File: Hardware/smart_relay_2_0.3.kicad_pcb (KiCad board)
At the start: 2 copper layers, 39 parts, among them J1 UART1 PROGRAMMER, J3 Conn_01x07_Pin, K1 PB766-ND, K2 PB766-ND, Q1 NPN, Q2 NPN, Q3 NPN, Q4 NPN, U1 ESP32-WROOM-32E-N8, U2 Reg linear 3.3v

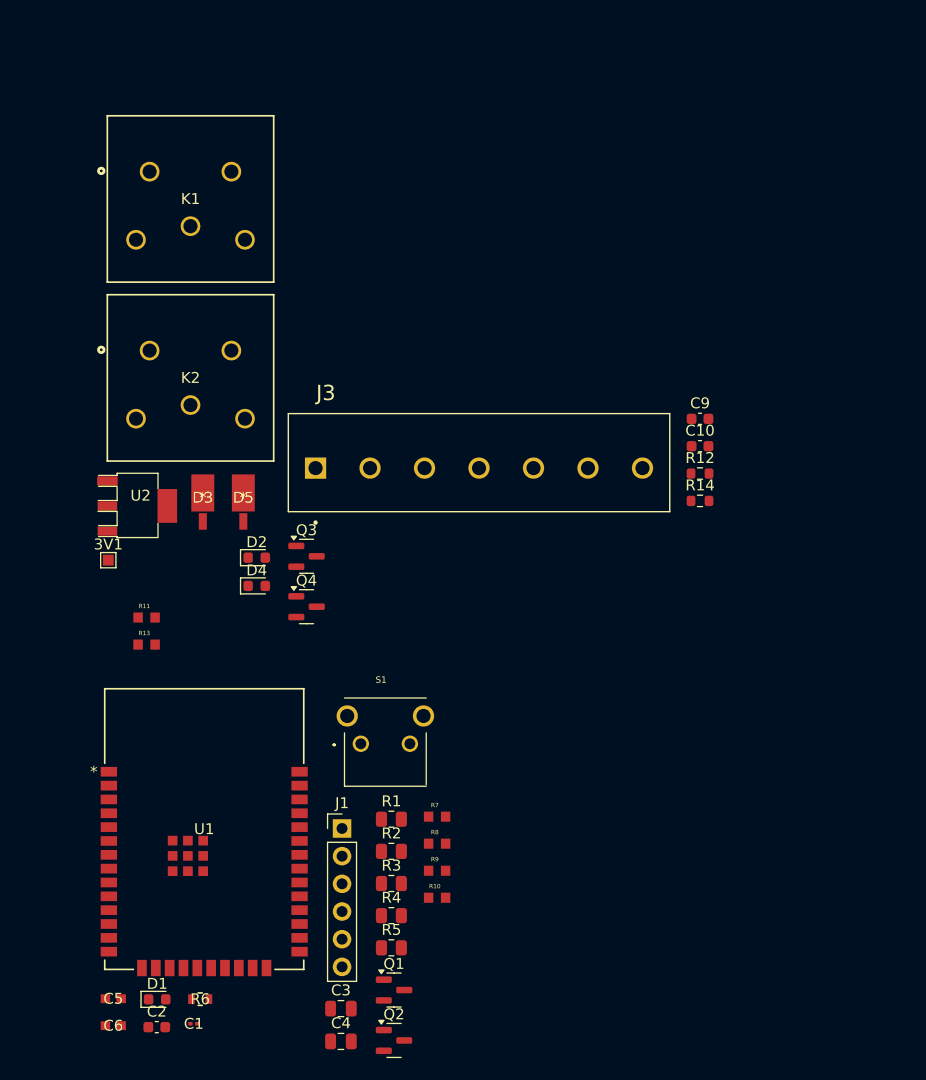
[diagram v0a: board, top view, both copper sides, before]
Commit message: strarted PCB placement for Smart relay v0_3
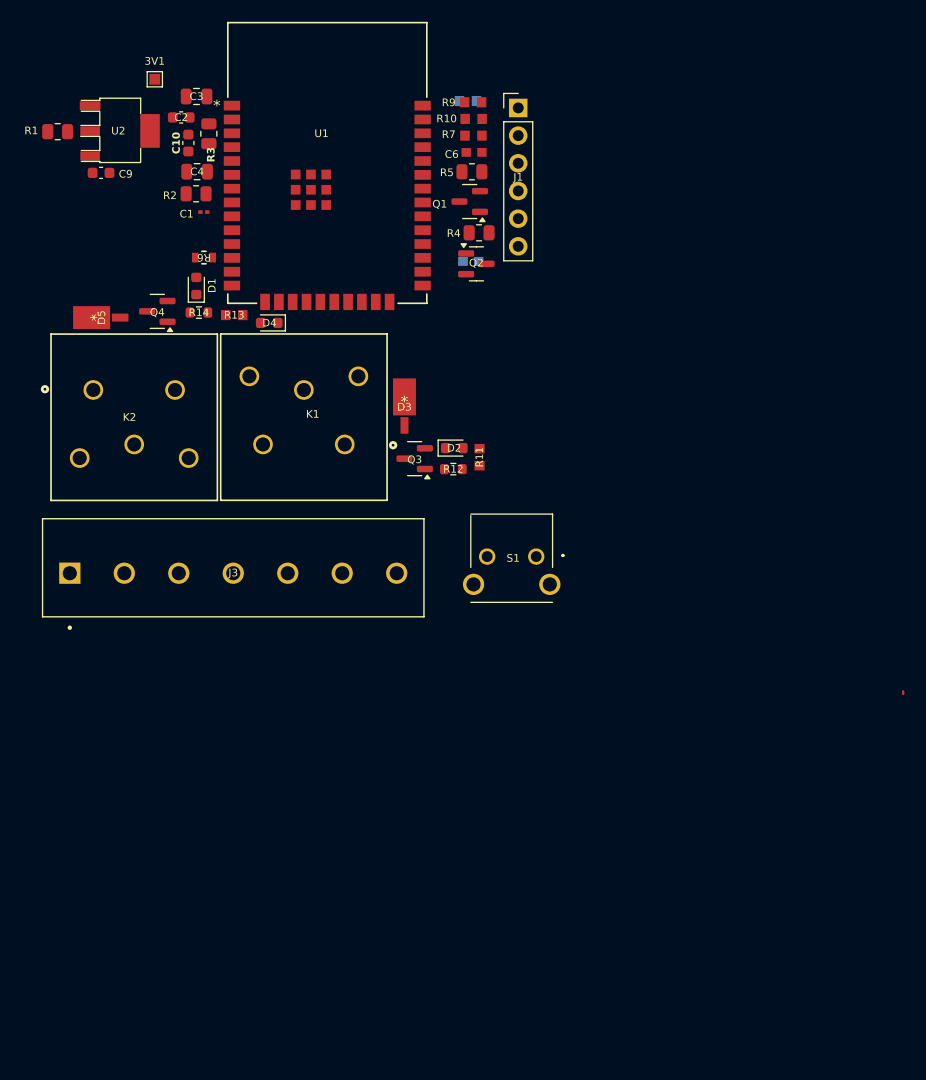
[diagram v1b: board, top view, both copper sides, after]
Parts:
- C5, R8: moved to B.Cu
- moved C6 86.7 mm to (96.4, 47.5)
- moved C3 84.7 mm to (70.9, 42.4), turned to 180 degrees
- moved C2 83.5 mm to (69.5, 44.3), turned to 180 degrees
- moved C4 80.9 mm to (71.0, 49.3), turned to 180 degrees
- moved C5 75.2 mm to (96.1, 57.5)
- moved C1 74.5 mm to (71.6, 53.0), turned to 180 degrees
- moved Q1 72.7 mm to (96.0, 52.0), turned to 180 degrees
- moved Q2 71.7 mm to (96.6, 57.7)
- moved R5 71.6 mm to (96.2, 49.3), turned to 180 degrees
- moved R10 71.5 mm to (96.4, 44.4)
- moved R3 70.8 mm to (72.1, 45.8), turned to -90 degrees
- moved R9 70.6 mm to (96.3, 42.9)
- moved R1 70.1 mm to (58.2, 45.6), turned to 180 degrees
- moved R8 68.2 mm to (95.8, 42.8), turned to 180 degrees
- moved J1 68.1 mm to (100.5, 43.4)
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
